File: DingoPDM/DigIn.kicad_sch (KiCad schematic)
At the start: 24 parts

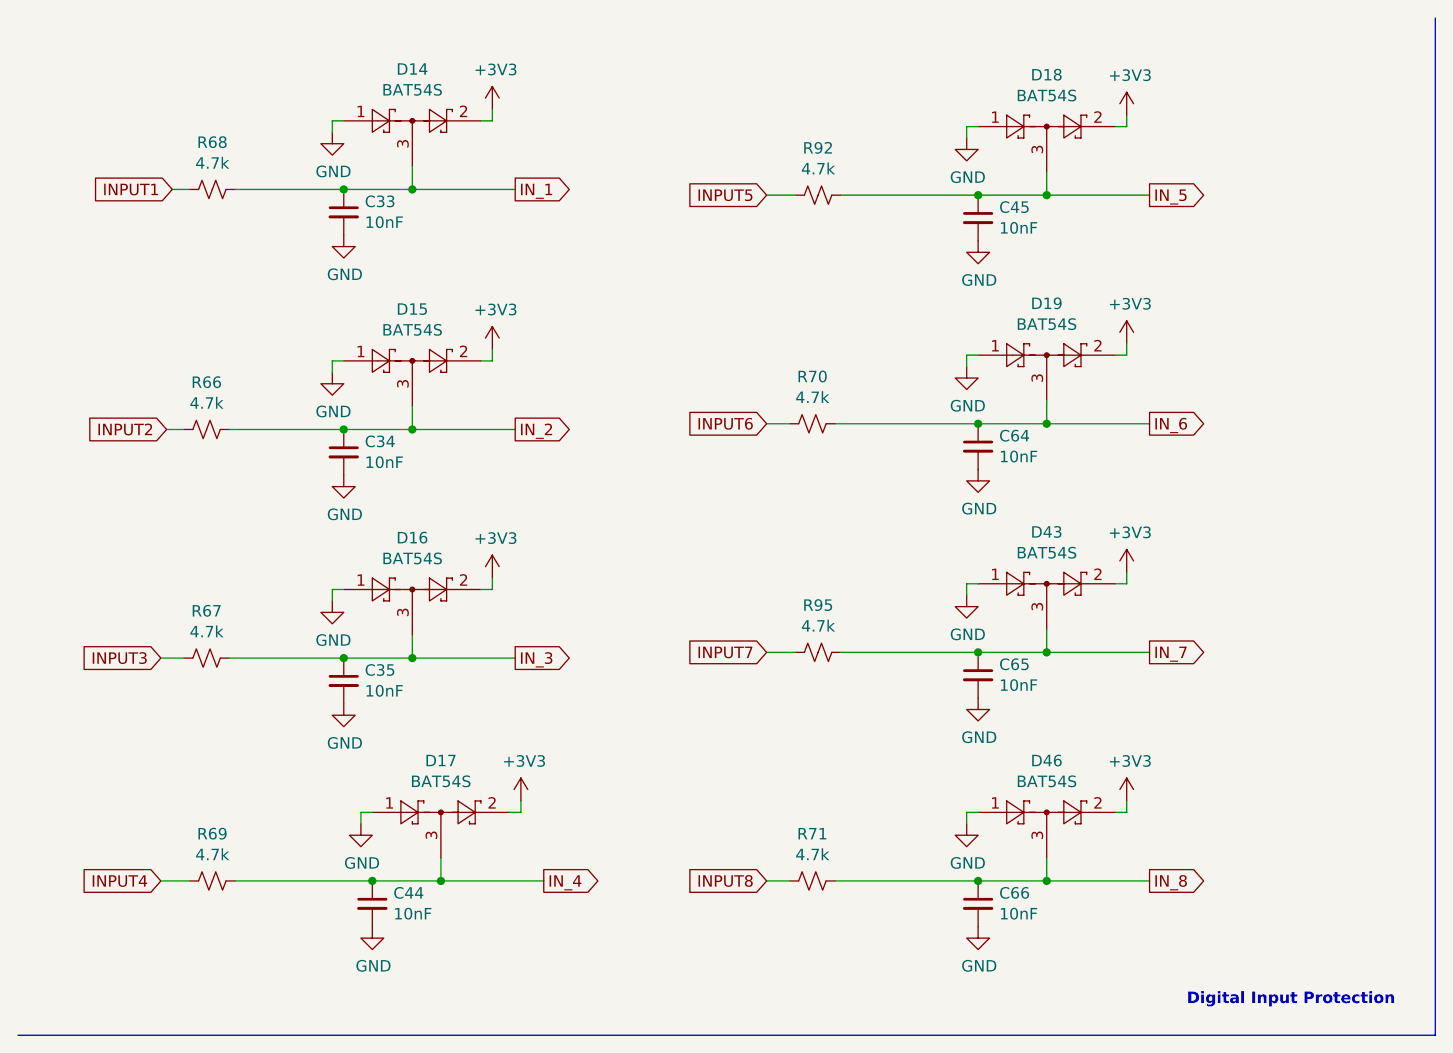
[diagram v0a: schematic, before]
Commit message: Swapped to AMPSEAL 14 pins
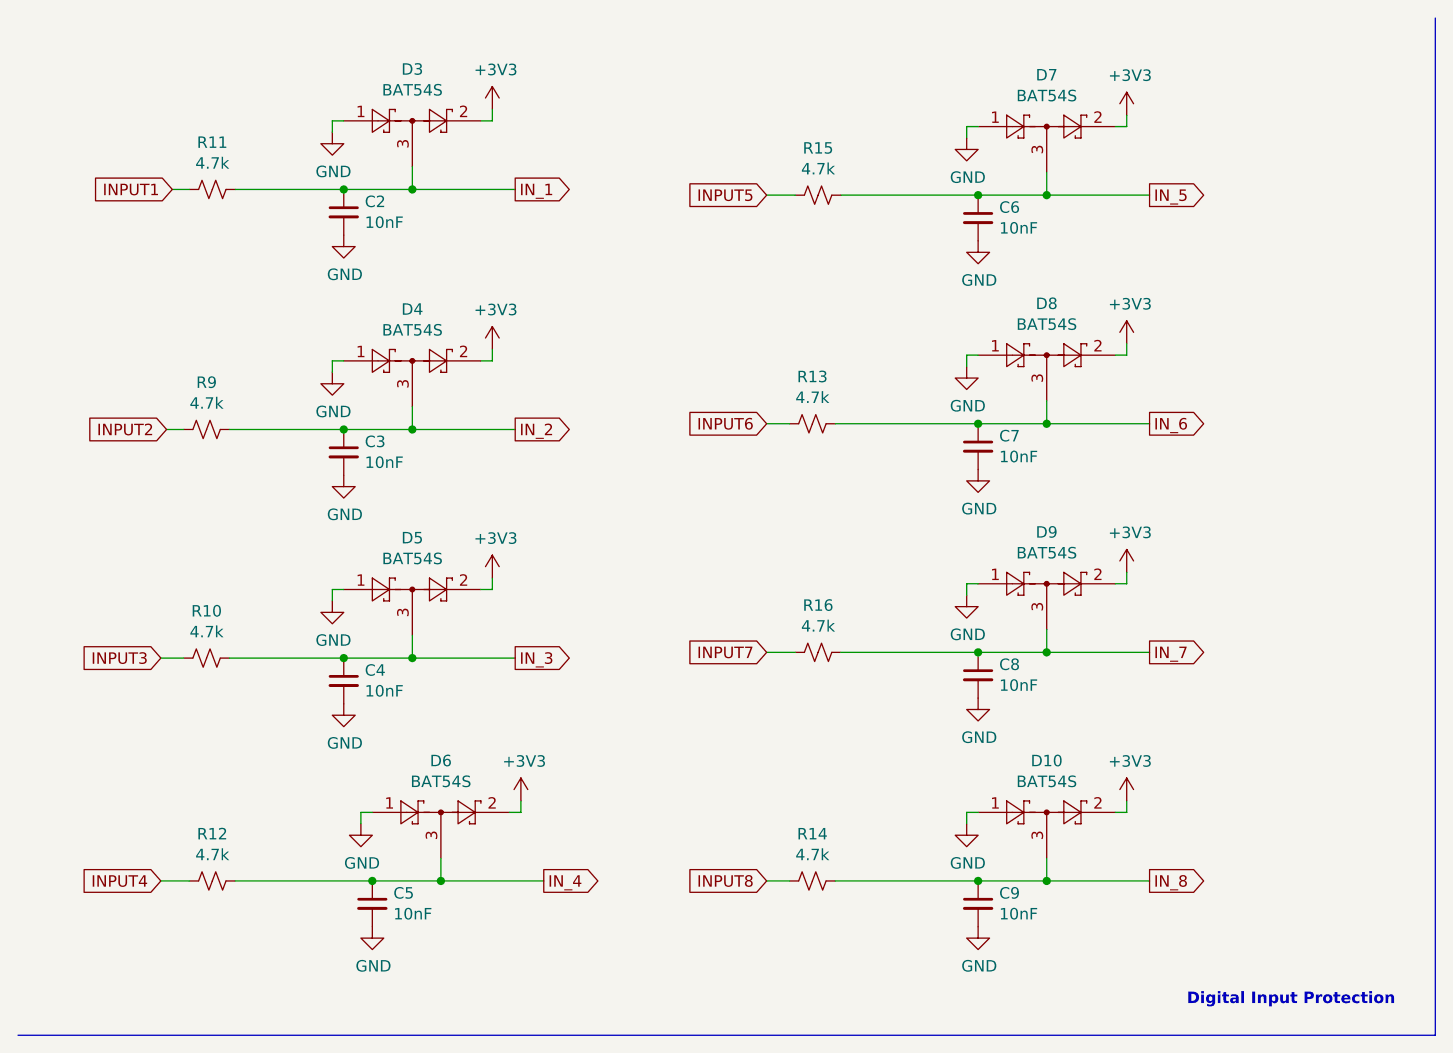
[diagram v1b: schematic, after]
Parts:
- renumbered C33 to C2, C34 to C3, C35 to C4, C44 to C5, C45 to C6, C64 to C7, C65 to C8, C66 to C9, D46 to D10, D14 to D3, D15 to D4, D16 to D5, D17 to D6, D18 to D7, D19 to D8, D43 to D9, R67 to R10, R68 to R11, R69 to R12, R70 to R13, R71 to R14, R92 to R15, R95 to R16, R66 to R9

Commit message: V5 As Built
-Changed ADS1015 to MAX11613EUA+T due to supply issues
-Changed PCB to match JLCPCB 2oz rules
-Changed ON_SW input to 12V switched
-Switched to TagConnect TC2030
-Changed pin positions of GND, IN1, IN2
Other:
- title: (none) -> Dingo_PDM
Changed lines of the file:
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@@
 (kicad_sch (version 20230121) (generator eeschema)
   (paper "A4")
+  (title_block
+    (title "Dingo_PDM")
+    (date "2023-02-23")
+    (rev "v5")
+    (comment 3 "github.com/corygrant")
+    (comment 4 "Cory Grant")
+  )
   (junction (at 118.745 107.95) (diameter 0) (color 0 0 0 0)
   )

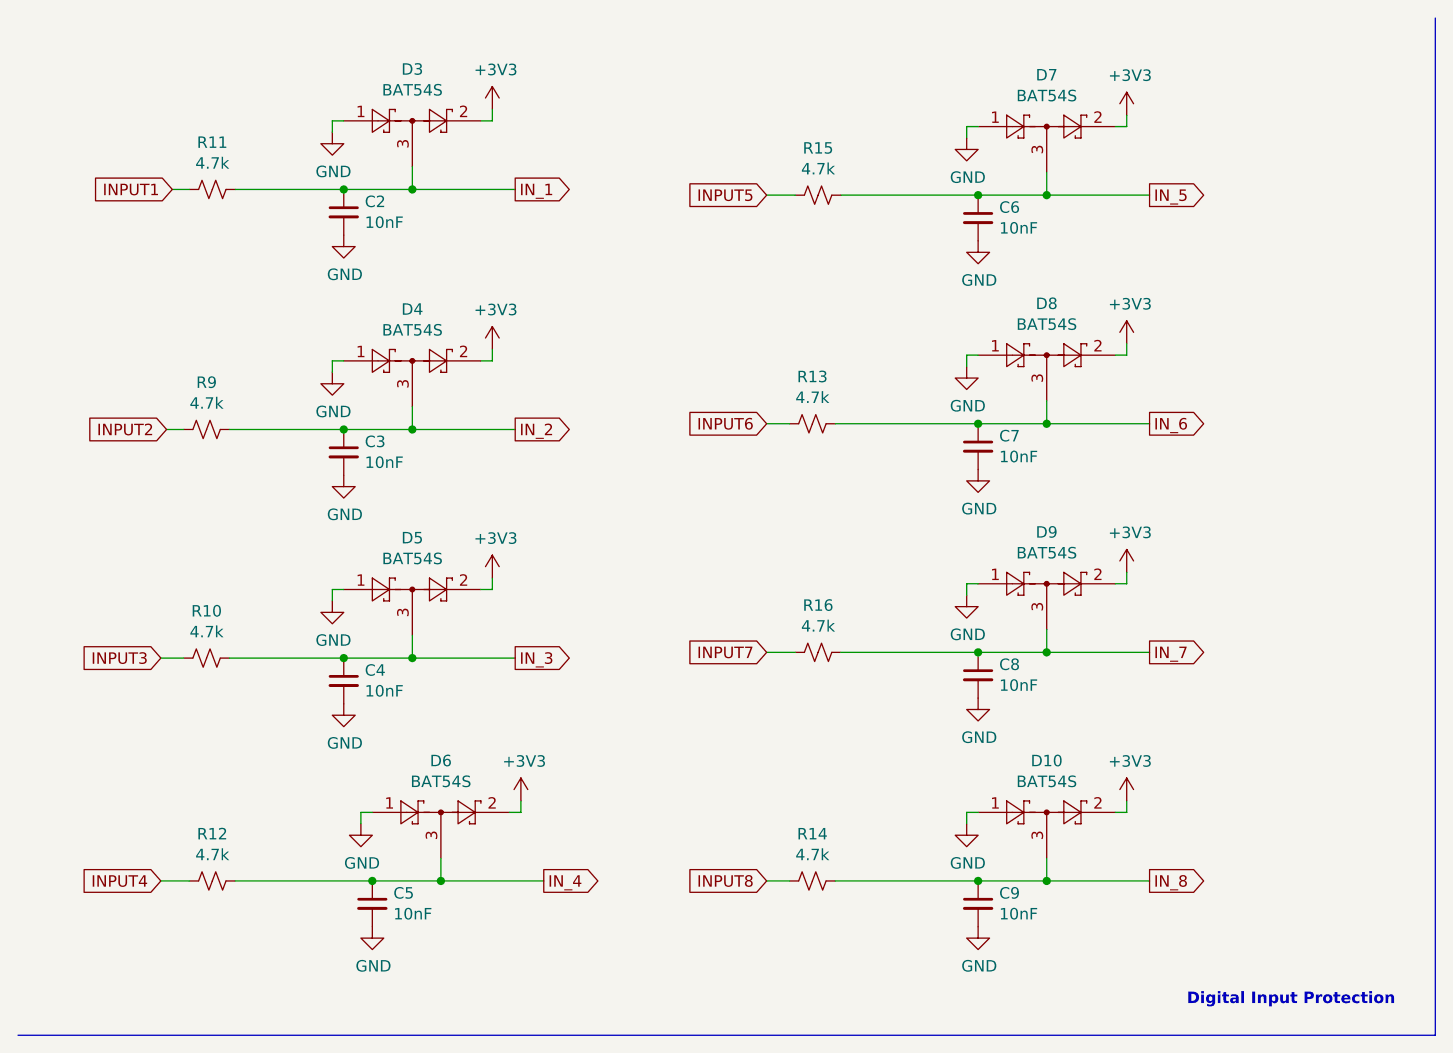
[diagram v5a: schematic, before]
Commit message: Redesigned to a smaller unit
4x high current, 2x med current, 4x low current, 2x digital inputs
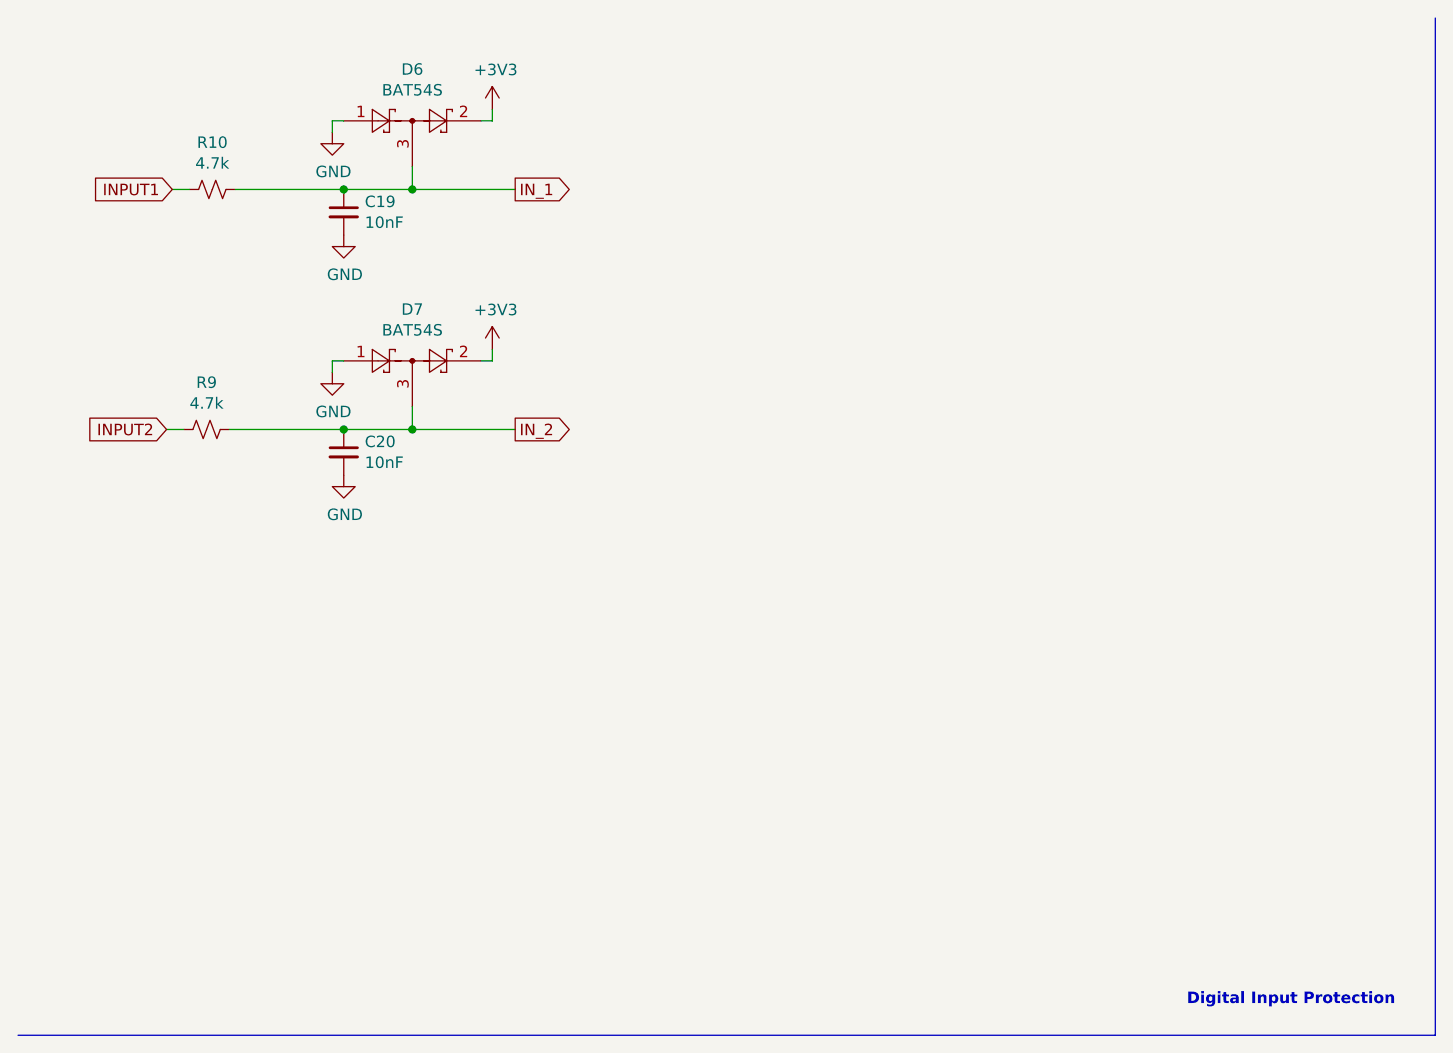
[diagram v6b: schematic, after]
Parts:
- removed C4, C5, C6, C7, C8, C9: 10nF, Capacitor_SMD:C_0805_2012Metric, symbol Device:C_Small
- removed D10, D5, D6, D7, D8, D9: BAT54S, Package_TO_SOT_SMD:SOT-23, symbol Diode:BAT54S
- removed R10, R12, R13, R14, R15, R16: 4.7k, Resistor_SMD:R_0805_2012Metric, symbol Device:R_Small_US
- C19: renamed from C2; LCSC (none) -> C1710
- C20: renamed from C3; LCSC (none) -> C1710
- D6: renamed from D3; LCSC (none) -> C47546
- D7: renamed from D4; LCSC (none) -> C47546
- R10: renamed from R11; LCSC (none) -> C17673
- R9: LCSC (none) -> C17673

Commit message: Added documentation, finished and cleaned design
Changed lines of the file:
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@@
   (title_block
     (title "Dingo_PDM")
-    (date "2023-04-01")
-    (rev "v5")
+    (date "2023-07-28")
+    (rev "v6")
     (comment 3 "github.com/corygrant")
     (comment 4 "Cory Grant")
@@
     (stroke (width 0) (type default))
   )
-  (polyline (pts (xy 169.545 12.065) (xy 169.545 125.095))
+  (polyline (pts (xy 88.265 12.065) (xy 88.265 75.565))
     (stroke (width 0) (type default))
   )
@@
     (stroke (width 0) (type default))
   )
-  (polyline (pts (xy 169.545 125.095) (xy 12.065 125.095))
+  (polyline (pts (xy 88.265 75.565) (xy 12.065 75.565))
     (stroke (width 0) (type default))
   )
@@
     (stroke (width 0) (type default))
   )
-  (text "Digital Input Protection" (at 165.1 121.92 0)
+  (text "Digital Input Protection" (at 86.995 73.025 0)
     (effects (font (size 1.27 1.27) (thickness 0.254) bold) (justify right bottom))
   )

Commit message: Routed V7
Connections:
- net INPUT1: now also R9.2; no longer R10.2
- net INPUT2: now also R10.2; no longer R9.2
- net IN_1: now also C20.1, D7.3, R9.1; no longer C19.1, D6.3, R10.1
- net IN_2: now also C19.1, D6.3, R10.1; no longer C20.1, D7.3, R9.1
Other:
- moved on the sheet: C19, C20, D6, D7, R10, R9
